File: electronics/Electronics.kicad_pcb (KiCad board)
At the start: 4 copper layers, 102.4 x 75 mm, 85 parts, among them J16 10118193-0001LF, J2 3mm_pad, J4 3mm_pad, Q1 BUK6Y10-30P, U1 STM32G441KBT3, U10 CM1223-02SO, U2 MAX14930DASE+, U3 MAX14930DASE+, U4 MAX14930DASE+, U5 DRV8243, U6 DRV8243, U7 DRV8243, U8 TPS54227DDAR, U9 NCP164

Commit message: Typo fix
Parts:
- renumbered MOT1 to MOT3

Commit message: Fixus trace
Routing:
- net +5VD: track 148.0 -> 144.1 mm
- net +3V3: track 215.6 -> 217.1 mm

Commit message: Spurdo v2.1 update
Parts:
- added C32: 0.1uF, Capacitor_SMD:C_0603_1608Metric_Pad1.08x0.95mm_HandSolder, F.Cu at (113.2, 96.7)
- moved C29 18.7 mm to (100.6, 75.0), turned to 90 degrees
- moved C27 17.2 mm to (76.0, 80.2)
- moved R14 17.2 mm to (76.0, 78.7)
- moved R15 17.2 mm to (76.0, 81.7)
- moved R16 17.2 mm to (76.0, 83.2)
- moved C23 16.9 mm to (76.0, 84.7)
- moved C28 15.1 mm to (99.9, 84.7)
- moved C20 14.8 mm to (89.9, 79.1)
- moved C26 14.7 mm to (89.9, 82.4)
- moved U8 14.7 mm to (85.3, 82.5)
- moved C19 14.3 mm to (84.8, 74.5), turned to 90 degrees
- moved C21 12.9 mm to (80.0, 83.1)
- moved L1 4.83 mm to (94.9, 83.3), turned to 0 degrees
- moved C14 1.75 mm to (124.4, 60.5), turned to 270 degrees
- moved C3 0.70 mm to (116.8, 97.2)
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- renumbered MOT1 to J1, Thrower to J10, Hold to J11, Aim to J12, BAT+ to J13, BAT- to J14, Debug to J15, MOT2 to J3, MOT3 to J5, MOT3 to J6, MOT1 to J7, MOT2 to J8, MOT3 to J9
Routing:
- net Vdrive: track 239.0 -> 188.4 mm
- net Earth: track 50.5 -> 30.6 mm, vias 27 -> 87
- net /Driver/MOT1en_2: track 54.3 -> 41.0 mm, vias 3 -> 2
- net /Driver/MOT_sleep: track 116.2 -> 106.5 mm, vias 6 -> 7
- net +5VD: track 144.1 -> 134.6 mm
- net Net-(C12-Pad2): track 15.1 -> 8.69 mm
- net Net-(C26-Pad2): track 8.85 -> 3.71 mm
- net GND: track 24.6 -> 29.3 mm, vias 20 -> 41
- net +3V3: track 217.1 -> 213.3 mm
- net /Driver/MOT_off: track 98.9 -> 102.7 mm, vias 6 -> 5
- net /MCU_NRST: track 41.8 -> 45.2 mm
- net Net-(C27-Pad1): track 6.49 -> 8.75 mm
- net Net-(R14-Pad2): track 4.24 -> 6.45 mm
- net Net-(C21-Pad2): track 3.77 -> 1.69 mm
- net /MCU-Hold-serv_PWM: track 37.0 -> 39.1 mm
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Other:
- rule via_min_size: 0.4 -> 0.6

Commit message: Silk fixes
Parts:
- moved D2 0.10 mm to (105.5, 116.2)
- moved R2 0.10 mm to (101.9, 116.2)
- renumbered J12 to Aim, J13 to BAT+, J14 to BAT-, J15 to Debug, J11 to Hold, J1 to MOT1, J7 to MOT1, J3 to MOT2, J8 to MOT2, J6 to MOT3, J9 to MOT3, J10 to Thrower

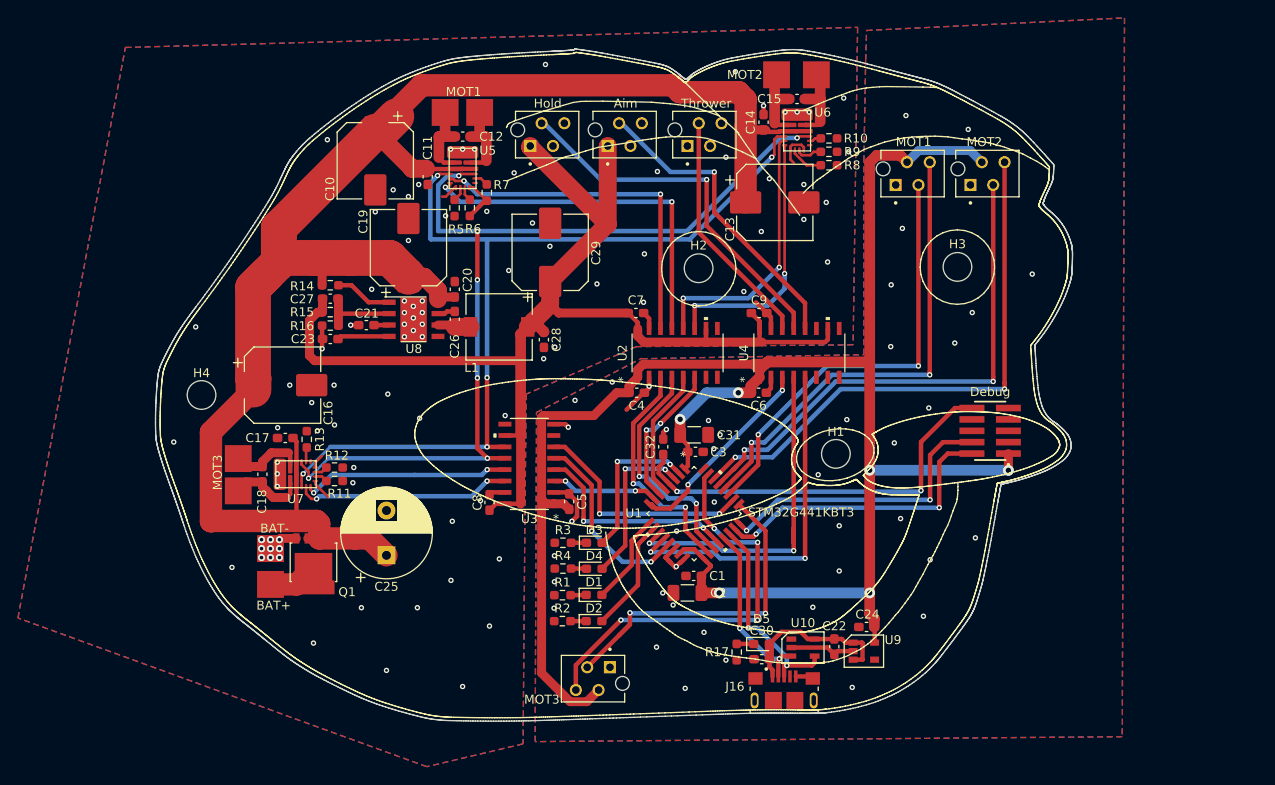
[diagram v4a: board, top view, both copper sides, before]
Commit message: Added vias
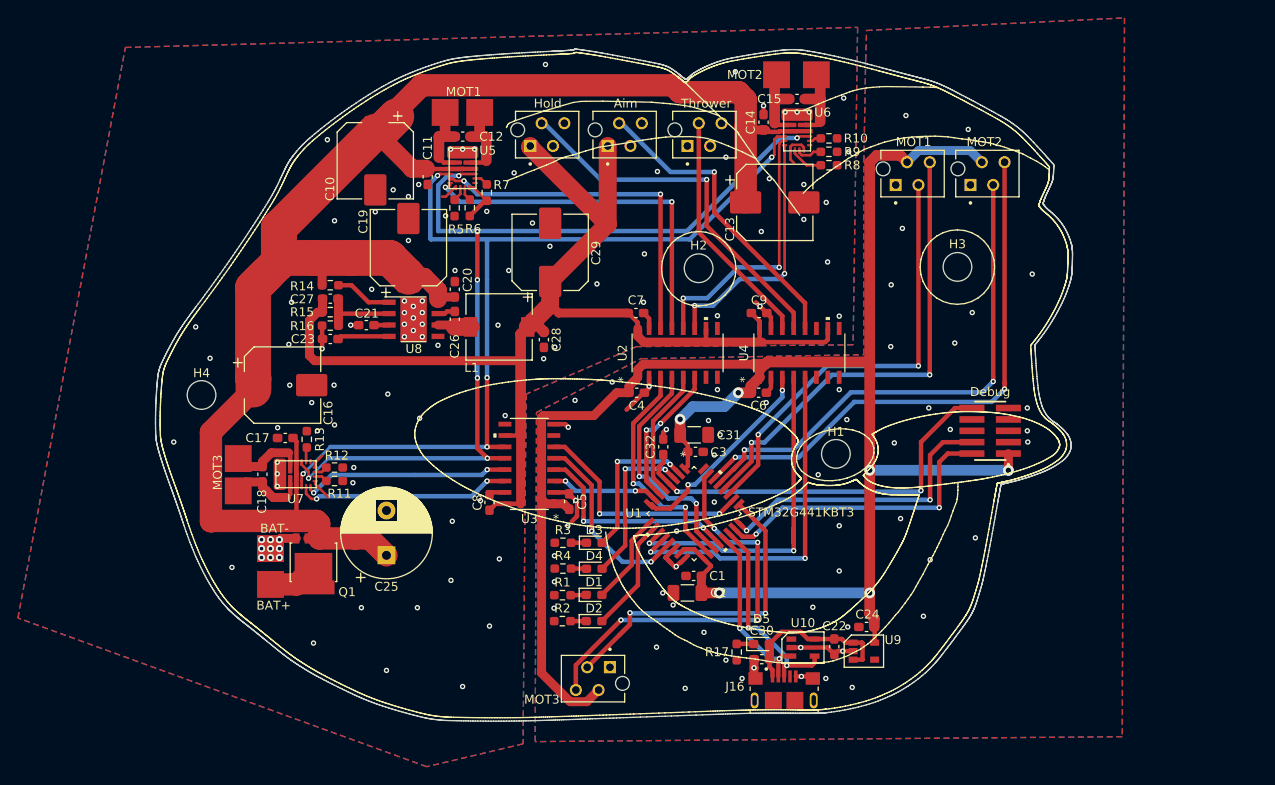
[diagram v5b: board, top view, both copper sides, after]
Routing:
- net GND: track 29.3 -> 31.4 mm, vias 41 -> 56
- net /Driver/MOT2en_2: track 29.4 -> 28.4 mm
- net Earth: vias 87 -> 96

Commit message: Updated dates and rev nr
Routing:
- net GND: track 31.4 -> 35.3 mm
